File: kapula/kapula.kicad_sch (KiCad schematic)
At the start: 153 parts, among them J1 Conn_02x10_Odd_Even, J12 U.FL, J13 U.FL, J3 Conn_02x10_Odd_Even, J4 Conn_ARM_JTAG_SWD_10, J5 U.FL, J9 U.FL, Q1 AO3401A, Q1 BSS84, Q2 AO3401A, Q3 AO3400A, Q5 AO3400A, Q6 AO3400A, T1 BW21S7511A01TF, T2 BW21S7511A01TF, T3 BW21S7511A01TF, T4 BW21S7511A01TF, U1 XC6206P332MR, U2 TP4054, U3 DW01+G, U5 EFR32FG14P233F256GM48-B, U6 XA213-G4J, X1 DSB221SDN, Y1 32768 Hz

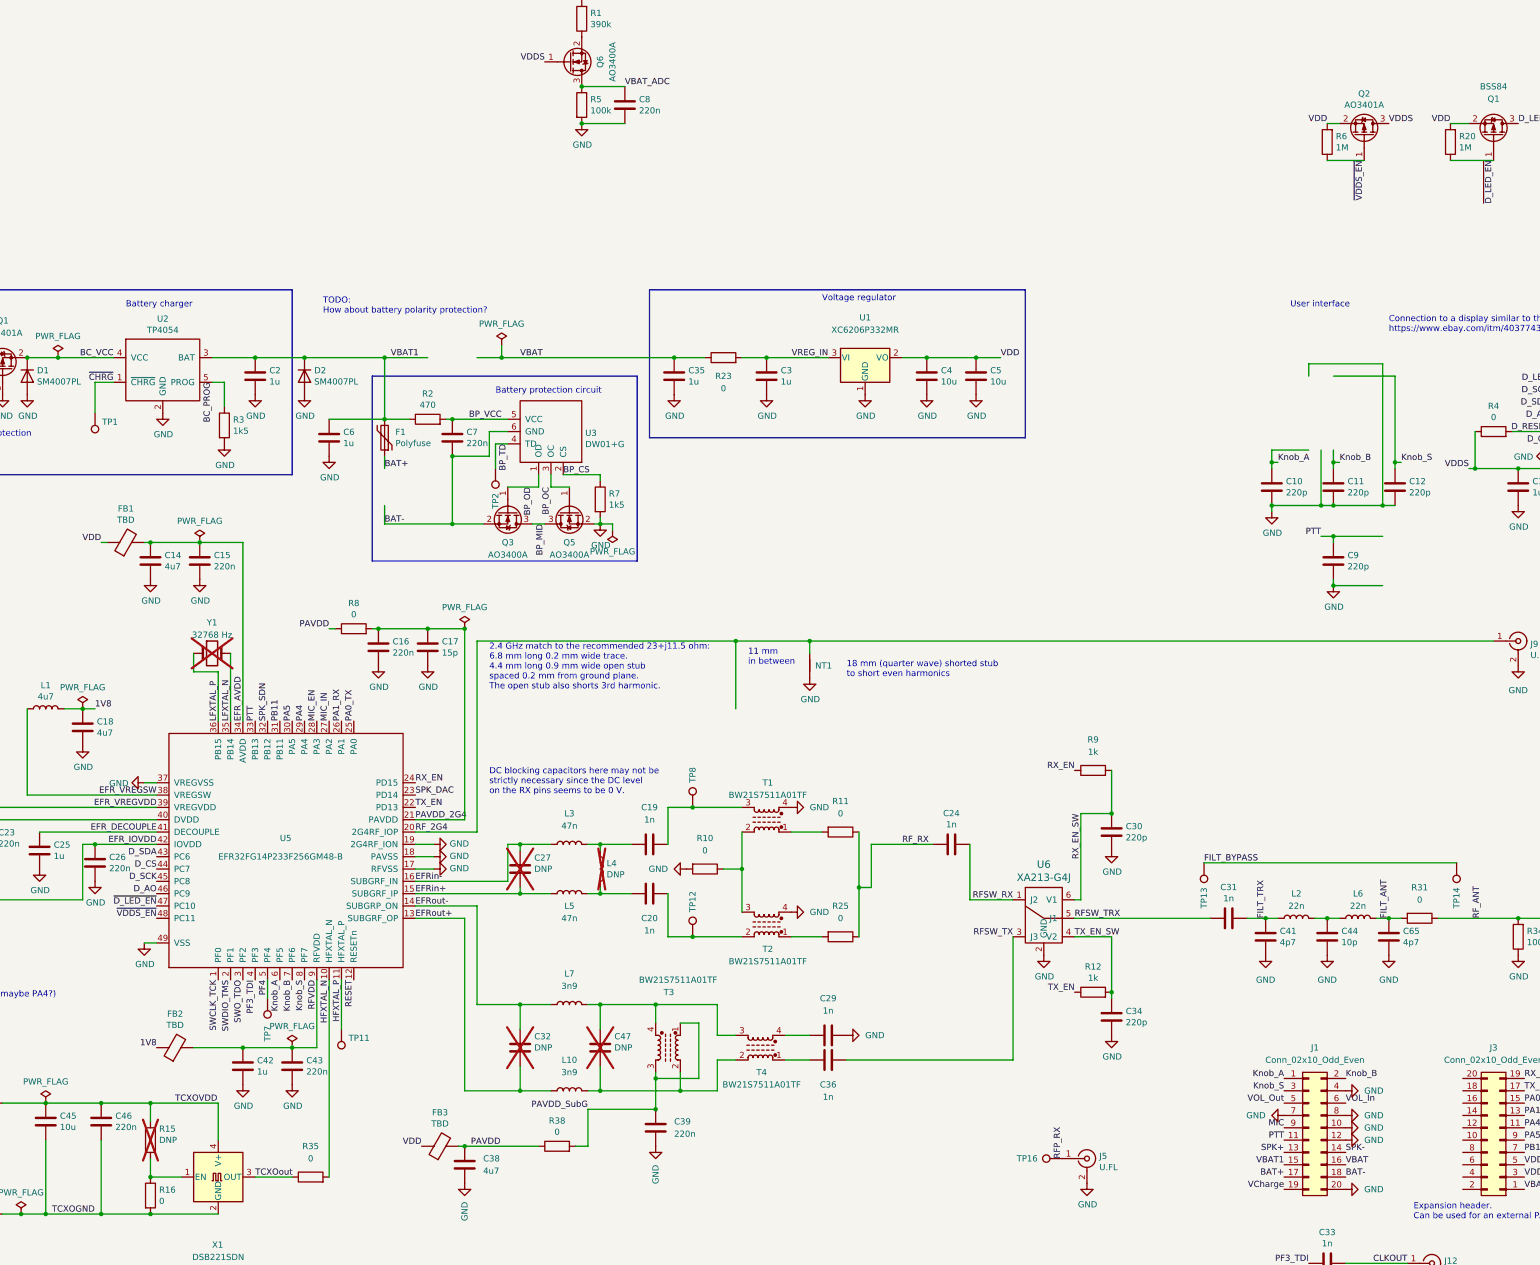
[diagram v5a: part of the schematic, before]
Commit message: PCB: Route PAVDD etc, change 2.4 GHz matching layout to make more space
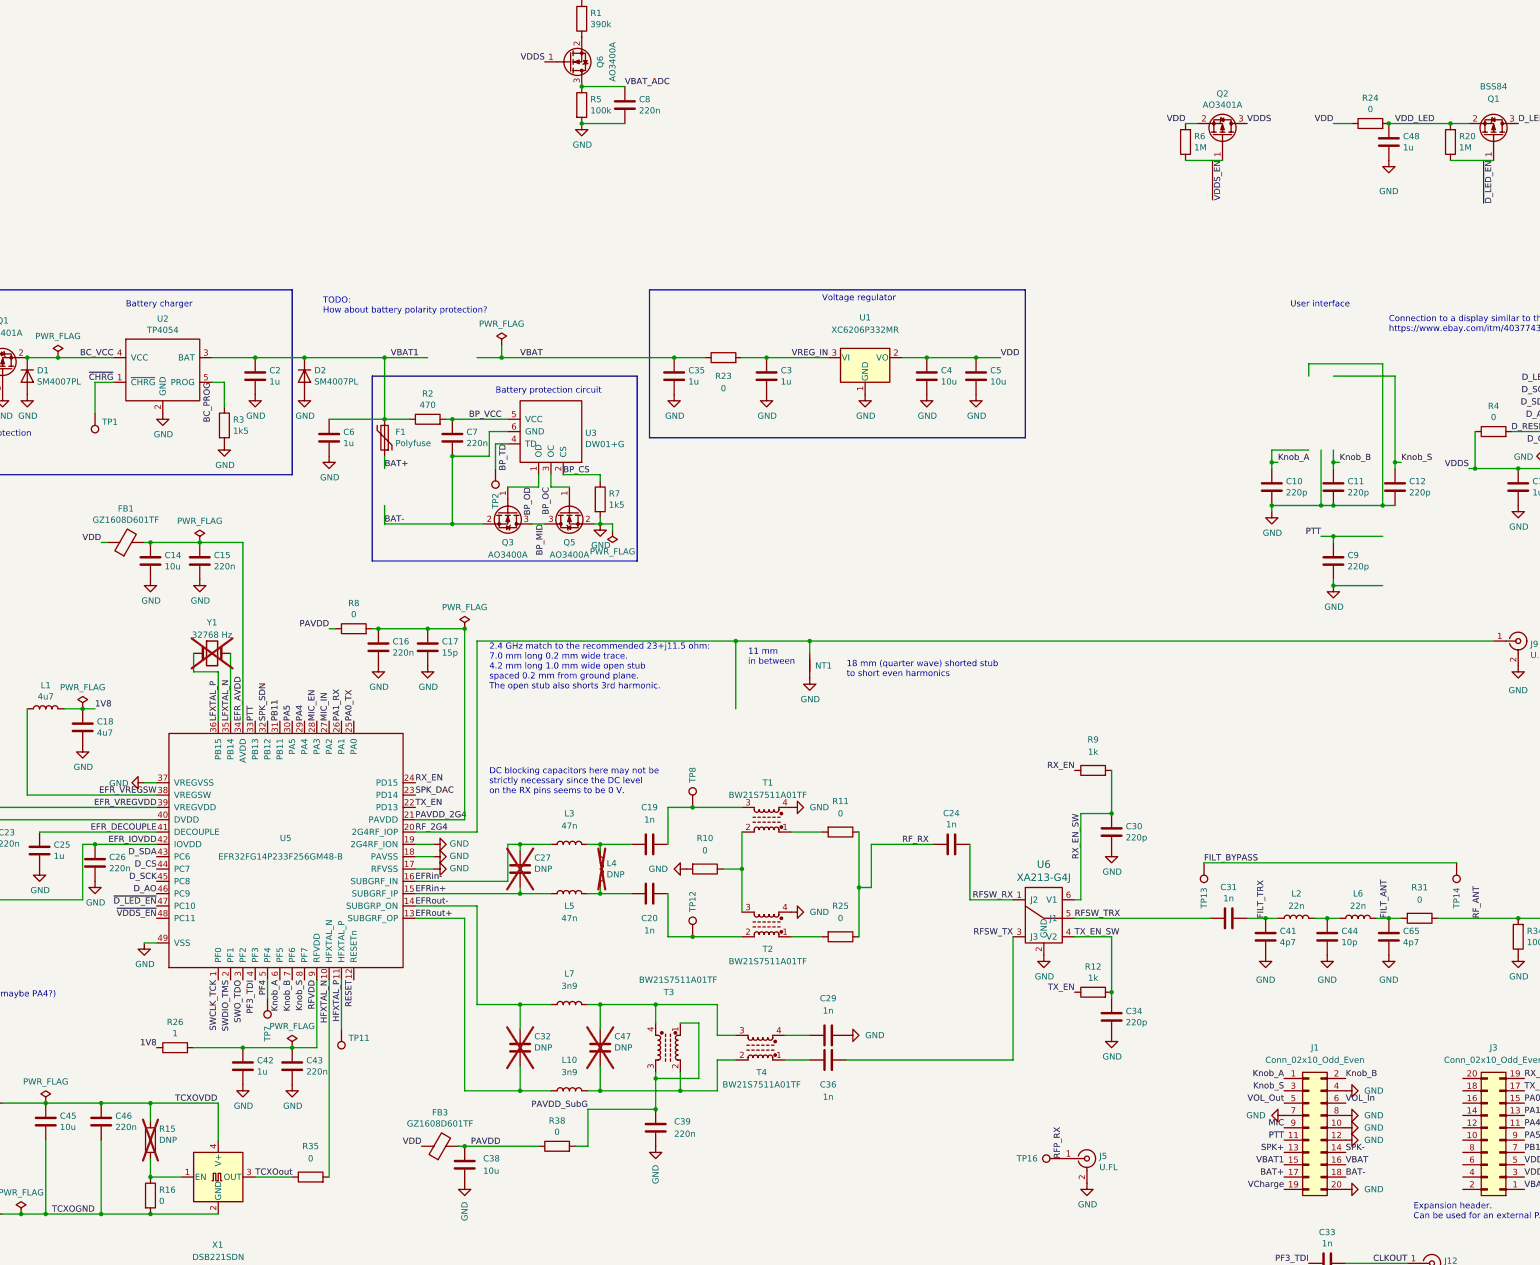
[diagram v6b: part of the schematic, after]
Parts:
- removed FB2: TBD, Inductor_SMD:L_0603_1608Metric_Pad1.05x0.95mm_HandSolder, symbol kapula-rescue:Ferrite_Bead-Device
- added C48: 1u, Capacitor_SMD:C_0603_1608Metric, symbol Device:C
- added R24: 0, Resistor_SMD:R_0402_1005Metric, symbol Device:R
- added R26: 1, kapula:R_0402_to_0603_HandSolder, symbol Device:R
- C14, C38: value 4u7 -> 10u; LCSC C1779 -> (none)
- FB1: value TBD -> GZ1608D601TF
- FB3: value TBD -> GZ1608D601TF; footprint Inductor_SMD:L_0805_2012Metric_Pad1.05x1.20mm_HandSolder -> Inductor_SMD:L_0603_1608Metric_Pad1.05x0.95mm_HandSolder; LCSC TBD -> C1002
- NT1: footprint NetTie:NetTie-2_SMD_Pad0.5mm -> kapula:NetTie-2_SMD_Pad0.3mm
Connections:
- net 1V8: now also R26.1
- net GND: now also C48.2
- net RFVDD: now also R26.2
- net VDD: now also R24.1; no longer Q1.2 (S), R20.2
- new net VDD_LED: C48.1, Q1.2 (S), R20.2, R24.2
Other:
- note added: "2.4 GHz match to the recommended 23+j11.5 ohm: 7.0 mm long 0.2 mm wide trace. 4.2 mm long 1.0 mm wide open stub spaced 0.2 mm from ground plane. The open stub also shorts 3rd harmonic."
- note removed: "2.4 GHz match to the recommended 23+j11.5 ohm: 6.8 mm long 0.2 mm wide trace. 4.4 mm long 0.9 mm wide open stub spaced 0.2 mm from ground plane. The open stub also shorts 3rd harmonic."
- moved on the sheet: Q2, R6

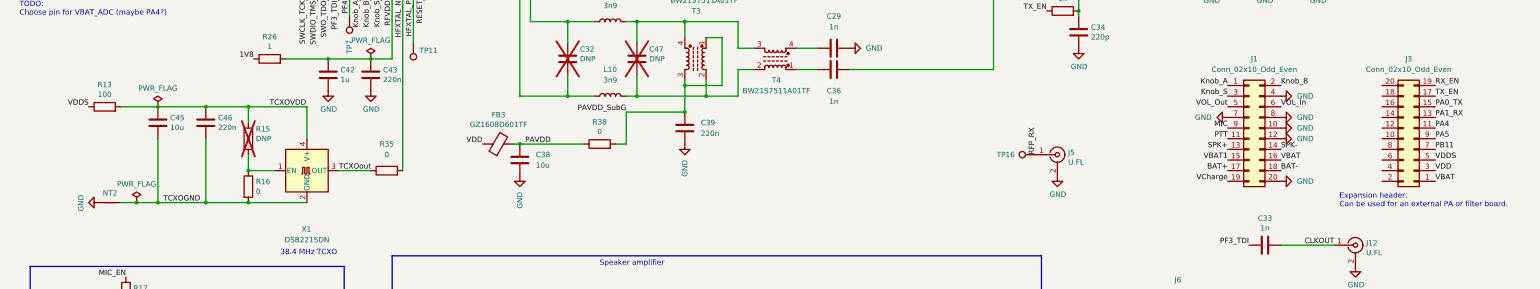
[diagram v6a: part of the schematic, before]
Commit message: PCB: Change TCXO to a more available one
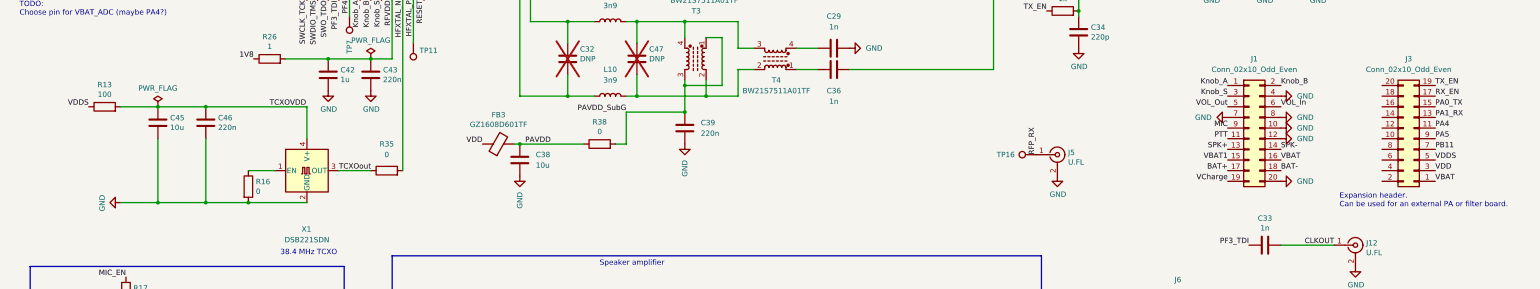
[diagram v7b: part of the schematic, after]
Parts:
- removed NT2: ~, NetTie:NetTie-2_SMD_Pad0.5mm, symbol kapula-rescue:Net-Tie_2-Device
- removed R15: DNP, kapula:R_0402_to_0603_HandSolder, symbol Device:R
- R16: footprint kapula:R_0402_to_0603_HandSolder -> Resistor_SMD:R_0402_1005Metric
- X1: footprint Oscillator:Oscillator_SMD_SeikoEpson_SG210-4Pin_2.5x2.0mm_HandSoldering -> kapula:TG2016SMN; LCSC C190737 -> C1987359
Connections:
- net TCXOGND is gone; now on net GND: C45.2, C46.2, R16.2, X1.2 (GND)
- net RX_EN: now also J3.17 (Pin_17); no longer J3.19 (Pin_19)
- net TX_EN: now also J3.19 (Pin_19); no longer J3.17 (Pin_17)
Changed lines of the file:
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@@
 (kicad_sch (version 20230121) (generator eeschema)
   (paper "A3")
-  (junction (at 109.22 180.34) (diameter 0) (color 0 0 0 0)
-  )
   (junction (at 171.45 60.96) (diameter 0) (color 0 0 0 0)
   )
@@
   (junction (at 219.71 261.62) (diameter 0) (color 0 0 0 0)
   )
-  (junction (at 109.22 195.58) (diameter 0) (color 0 0 0 0)
-  )
   (junction (at 53.34 119.38) (diameter 0) (color 0 0 0 0)
   )
@@
   (junction (at 171.45 46.99) (diameter 0) (color 0 0 0 0)
   )
-  (junction (at 82.55 203.2) (diameter 0) (color 0 0 0 0)
-  )
   (junction (at 340.36 57.15) (diameter 0) (color 0 0 0 0)
   )
@@
     (stroke (width 0) (type default))
   )
-  (wire (pts (xy 109.22 191.77) (xy 109.22 195.58))
-    (stroke (width 0) (type default))
-  )
   (wire (pts (xy 123.19 91.44) (xy 123.19 101.6))
     (stroke (width 0) (type default))
@@
     (stroke (width 0) (type default))
   )
-  (wire (pts (xy 109.22 180.34) (xy 99.06 180.34))
+  (wire (pts (xy 99.06 180.34) (xy 123.19 180.34))
     (stroke (width 0) (type default))
   )
@@
     (stroke (width 0) (type default))
   )
-  (wire (pts (xy 82.55 203.2) (xy 87.63 203.2))
-    (stroke (width 0) (type default))
-  )
   (wire (pts (xy 166.37 82.55) (xy 173.99 82.55))
     (stroke (width 0) (type default))
@@
     (stroke (width 0) (type default))
   )
-  (wire (pts (xy 109.22 184.15) (xy 109.22 180.34))
-    (stroke (width 0) (type default))
-  )
   (wire (pts (xy 173.99 189.23) (xy 189.23 189.23))
     (stroke (width 0) (type default))
@@
     (stroke (width 0) (type default))
   )
-  (wire (pts (xy 78.74 203.2) (xy 82.55 203.2))
+  (wire (pts (xy 78.74 203.2) (xy 87.63 203.2))
     (stroke (width 0) (type default))
   )
@@
     (stroke (width 0) (type default))
   )
-  (wire (pts (xy 109.22 180.34) (xy 123.19 180.34))
-    (stroke (width 0) (type default))
-  )
   (wire (pts (xy 201.93 59.69) (xy 201.93 60.96))
     (stroke (width 0) (type default))
@@
     (effects (font (size 1.27 1.27)) (justify left bottom))
   )
-  (label "TCXOGND" (at 88.9 203.2 0) (fields_autoplaced)
-    (effects (font (size 1.27 1.27)) (justify left bottom))
-  )
   (label "FILT_ANT" (at 364.49 142.24 90) (fields_autoplaced)
     (effects (font (size 1.27 1.27)) (justify left bottom))
@@
     (effects (font (size 1.27 1.27)) (justify left bottom))
   )
-  (label "RX_EN" (at 392.43 175.26 0) (fields_autoplaced)
+  (label "RX_EN" (at 392.43 177.8 0) (fields_autoplaced)
     (effects (font (size 1.27 1.27)) (justify left bottom))
   )
@@
     (effects (font (size 1.27 1.27)) (justify left bottom))
   )
-  (label "TX_EN" (at 392.43 177.8 0) (fields_autoplaced)
+  (label "TX_EN" (at 392.43 175.26 0) (fields_autoplaced)
     (effects (font (size 1.27 1.27)) (justify left bottom))
   )
@@
       (effects (font (size 1.27 1.27)))
     )
-    (property "Footprint" "Oscillator:Oscillator_SMD_SeikoEpson_SG210-4Pin_2.5x2.0mm_HandSoldering" (at 140.97 204.47 0)
+    (property "Footprint" "kapula:TG2016SMN" (at 140.97 204.47 0)
       (effects (font (size 1.27 1.27)) hide)
     )
-    (property "Datasheet" "https://datasheet.lcsc.com/szlcsc/1912111437_JGHC-TCO22384001805_C431173.pdf" (at 120.65 195.58 0)
+    (property "Datasheet" "https://datasheet.lcsc.com/lcsc/2206141530_Seiko-Epson-TG2016SMN-38-4000M-MCGNNM3_C1987359.pdf" (at 120.65 195.58 0)
       (effects (font (size 1.27 1.27)) hide)
     )
-    (property "LCSC" "C190737" (at 123.19 195.58 0)
+    (property "LCSC" "C1987359" (at 123.19 195.58 0)
       (effects (font (size 1.27 1.27)) hide)
     )
@@
     )
   )
-  (symbol (lib_id "power:GND") (at 73.66 203.2 270) (unit 1)
+  (symbol (lib_id "power:GND") (at 78.74 203.2 270) (unit 1)
     (in_bom yes) (on_board yes) (dnp no)
-    (property "Reference" "#PWR057" (at 67.31 203.2 0)
+    (property "Reference" "#PWR057" (at 72.39 203.2 0)
       (effects (font (size 1.27 1.27)) hide)
     )
-    (property "Value" "GND" (at 69.2658 203.327 0)
+    (property "Value" "GND" (at 74.3458 203.327 0)
       (effects (font (size 1.27 1.27)))
     )
-    (property "Footprint" "" (at 73.66 203.2 0)
+    (property "Footprint" "" (at 78.74 203.2 0)
       (effects (font (size 1.27 1.27)) hide)
     )
-    (property "Datasheet" "" (at 73.66 203.2 0)
+    (property "Datasheet" "" (at 78.74 203.2 0)
       (effects (font (size 1.27 1.27)) hide)
     )
@@
       (effects (font (size 1.27 1.27)) (justify left))
     )
-    (property "Footprint" "kapula:R_0402_to_0603_HandSolder" (at 107.442 199.39 90)
+    (property "Footprint" "Resistor_SMD:R_0402_1005Metric" (at 107.442 199.39 90)
       (effects (font (size 1.27 1.27)) hide)
     )
@@
     )
   )
-  (symbol (lib_id "Device:R") (at 109.22 187.96 0) (unit 1)
-    (in_bom no) (on_board yes) (dnp yes)
-    (property "Reference" "R15" (at 110.998 185.6486 0)
-      (effects (font (size 1.27 1.27)) (justify left))
-    )
-    (property "Value" "DNP" (at 110.998 187.96 0)
-      (effects (font (size 1.27 1.27)) (justify left))
-    )
-    (property "Footprint" "kapula:R_0402_to_0603_HandSolder" (at 107.442 187.96 90)
-      (effects (font (size 1.27 1.27)) hide)
-    )
-    (property "Datasheet" "" (at 109.22 187.96 0)
-      (effects (font (size 1.27 1.27)) hide)
-    )
-    (pin "1")
-    (pin "2")
-    (instances
-      (project "kapula"
-        (path "/f2315993-072e-45c9-8c85-e79c6d40aba4"
-          (reference "R15") (unit 1)
-        )
-      )
-    )
-  )
   (symbol (lib_id "Device:C") (at 307.34 162.56 0) (unit 1)
     (in_bom yes) (on_board yes) (dnp no)
@@
         )
       )
-    )
-  )
-  (symbol (lib_id "kapula-rescue:Net-Tie_2-Device") (at 76.2 203.2 0) (unit 1)
-    (in_bom yes) (on_board yes) (dnp no)
-    (property "Reference" "NT2" (at 76.2 200.9394 0)
-      (effects (font (size 1.27 1.27)))
-    )
-    (property "Value" "~" (at 77.343 202.0824 90)
-      (effects (font (size 1.27 1.27)) (justify left))
-    )
-    (property "Footprint" "NetTie:NetTie-2_SMD_Pad0.5mm" (at 76.2 203.2 0)
-      (effects (font (size 1.27 1.27)) hide)
-    )
-    (property "Datasheet" "" (at 76.2 203.2 0)
-      (effects (font (size 1.27 1.27)) hide)
-    )
-    (pin "1")
-    (pin "2")
-    (instances
-      (project "kapula"
-        (path "/f2315993-072e-45c9-8c85-e79c6d40aba4"
-          (reference "NT2") (unit 1)
-        )
-      )
-    )
-  )
-  (symbol (lib_id "power:PWR_FLAG") (at 82.55 203.2 0) (unit 1)
-    (in_bom yes) (on_board yes) (dnp no)
-    (property "Reference" "#FLG09" (at 82.55 201.295 0)
-      (effects (font (size 1.27 1.27)) hide)
-    )
-    (property "Value" "PWR_FLAG" (at 82.55 198.7804 0)
-      (effects (font (size 1.27 1.27)))
-    )
-    (property "Footprint" "" (at 82.55 203.2 0)
-      (effects (font (size 1.27 1.27)) hide)
-    )
-    (property "Datasheet" "~" (at 82.55 203.2 0)
-      (effects (font (size 1.27 1.27)) hide)
-    )
-    (pin "1")
-    (instances
-      (project "kapula"
-        (path "/f2315993-072e-45c9-8c85-e79c6d40aba4"
-          (reference "#FLG09") (unit 1)
-        )
-      )

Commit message: PCB: Try to make space for clock out connector
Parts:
- R36, R37: footprint kapula:R_0402_to_0603_HandSolder -> Resistor_SMD:R_0402_1005Metric
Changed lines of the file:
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@@
       (effects (font (size 1.27 1.27)))
     )
-    (property "Footprint" "kapula:R_0402_to_0603_HandSolder" (at 29.21 121.158 90)
+    (property "Footprint" "Resistor_SMD:R_0402_1005Metric" (at 29.21 121.158 90)
       (effects (font (size 1.27 1.27)) hide)
     )
@@
       (effects (font (size 1.27 1.27)))
     )
-    (property "Footprint" "kapula:R_0402_to_0603_HandSolder" (at 29.21 140.208 90)
+    (property "Footprint" "Resistor_SMD:R_0402_1005Metric" (at 29.21 140.208 90)
       (effects (font (size 1.27 1.27)) hide)
     )
